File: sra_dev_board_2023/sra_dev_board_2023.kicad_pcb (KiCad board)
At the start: 2 copper layers, 81.2 x 92.7 mm, 201 parts, among them J1 Conn_01x19_Male, J10 Conn_01x03_Male, J11 Conn_01x05_Male, J12 Conn_01x05_Male, J13 Conn_01x05_Male, J14 Conn_01x03_Male, J15 Conn_01x03_Male, J16 Screw_Terminal_01x05, J17 Conn_01x06_Male, J2 Conn_01x03_Male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

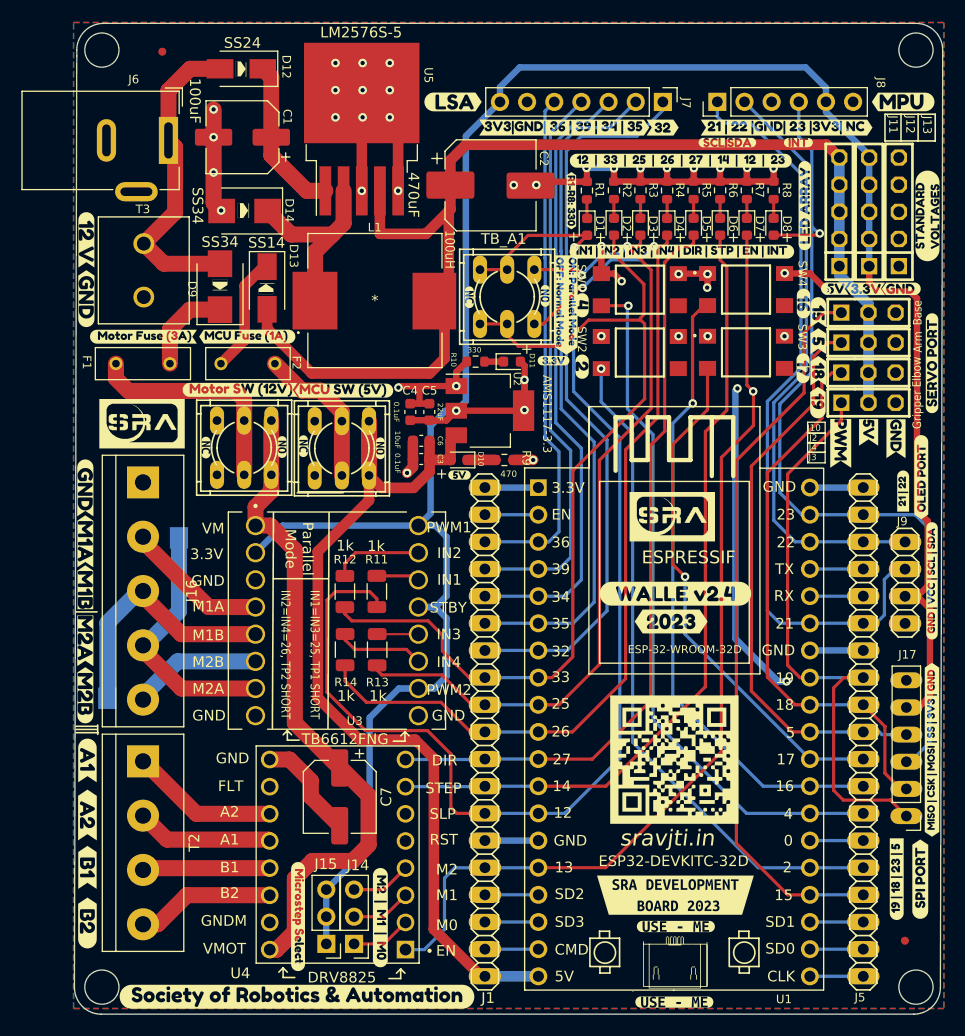
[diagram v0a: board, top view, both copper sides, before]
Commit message: Tweaks in routing prototype-1
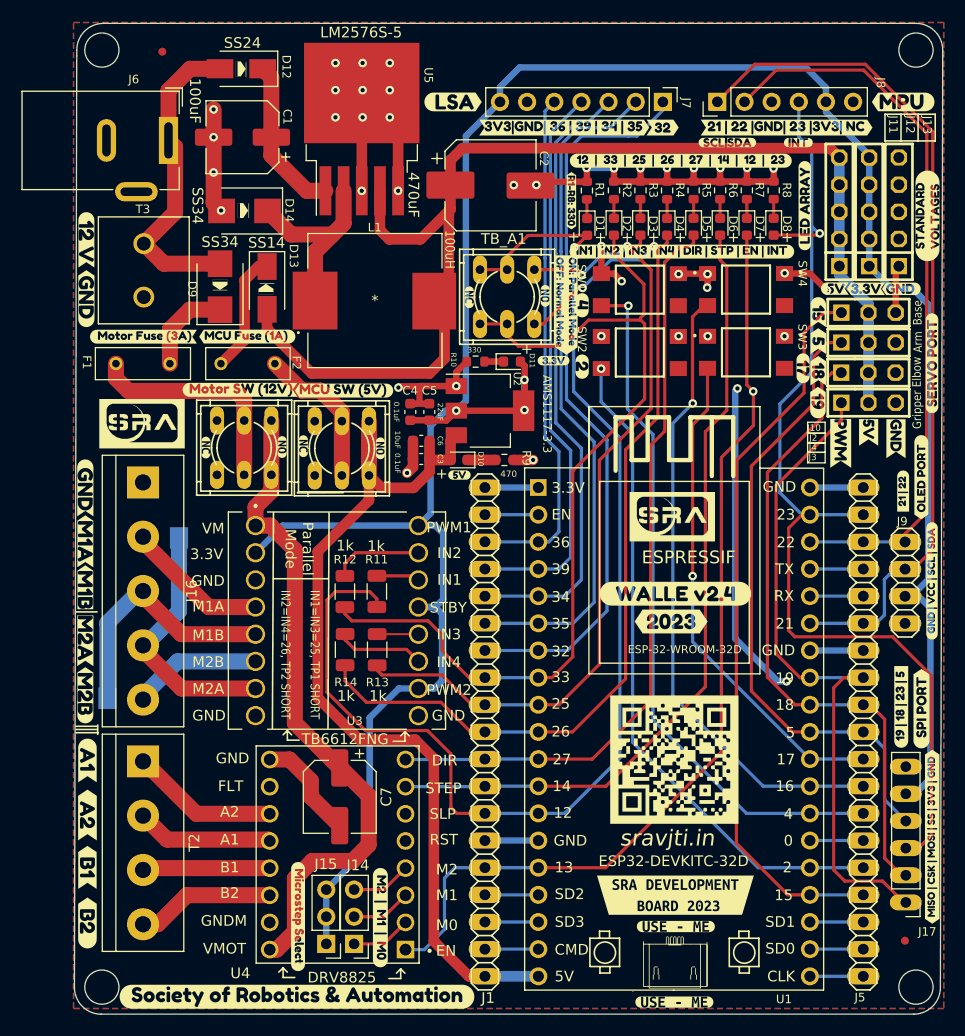
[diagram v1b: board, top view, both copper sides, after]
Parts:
- removed kibuzzard-61F6A06B: G***, kibuzzard-61F6A06B
- moved kibuzzard-637B65B8 16.7 mm to (147.2, 92.9)
- moved kibuzzard-637A1556 16.1 mm to (147.1, 93.4)
- moved kibuzzard-637A19A6 16.0 mm to (149.0, 93.5)
- moved kibuzzard-63777F1B 16.0 mm to (149.1, 93.5)
- moved kibuzzard-63775DBB 8.13 mm to (150.0, 105.5)
- moved kibuzzard-63775DBB 8.10 mm to (150.0, 105.5)
- moved J17 8.08 mm to (147.6, 111.7)
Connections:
- net /21 renamed D+
- net /22 renamed D-
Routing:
- net /23: track 82.2 -> 97.6 mm
- net D-: track 55.9 -> 68.7 mm
- net D+: track 71.0 -> 80.0 mm
- net /19: track 54.8 -> 63.3 mm
- net /18: track 51.7 -> 60.1 mm
- net /3V3: track 230.8 -> 238.4 mm
- net /5: track 53.0 -> 59.1 mm
- net GND: track 148.3 -> 152.6 mm
- net /17: track 48.2 -> 46.7 mm
- net /5V_P: track 82.8 -> 83.5 mm

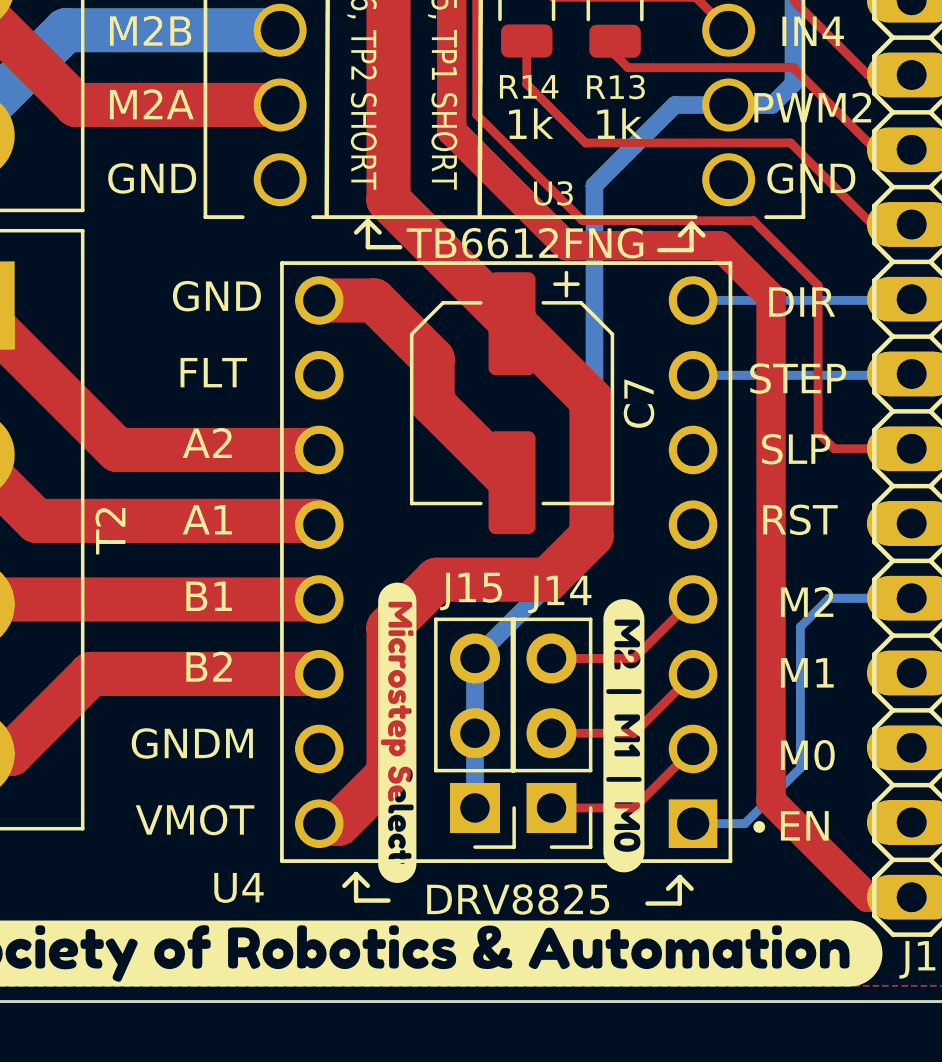
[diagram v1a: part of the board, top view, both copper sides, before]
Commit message: Update LSA and SRA board after hardware testing
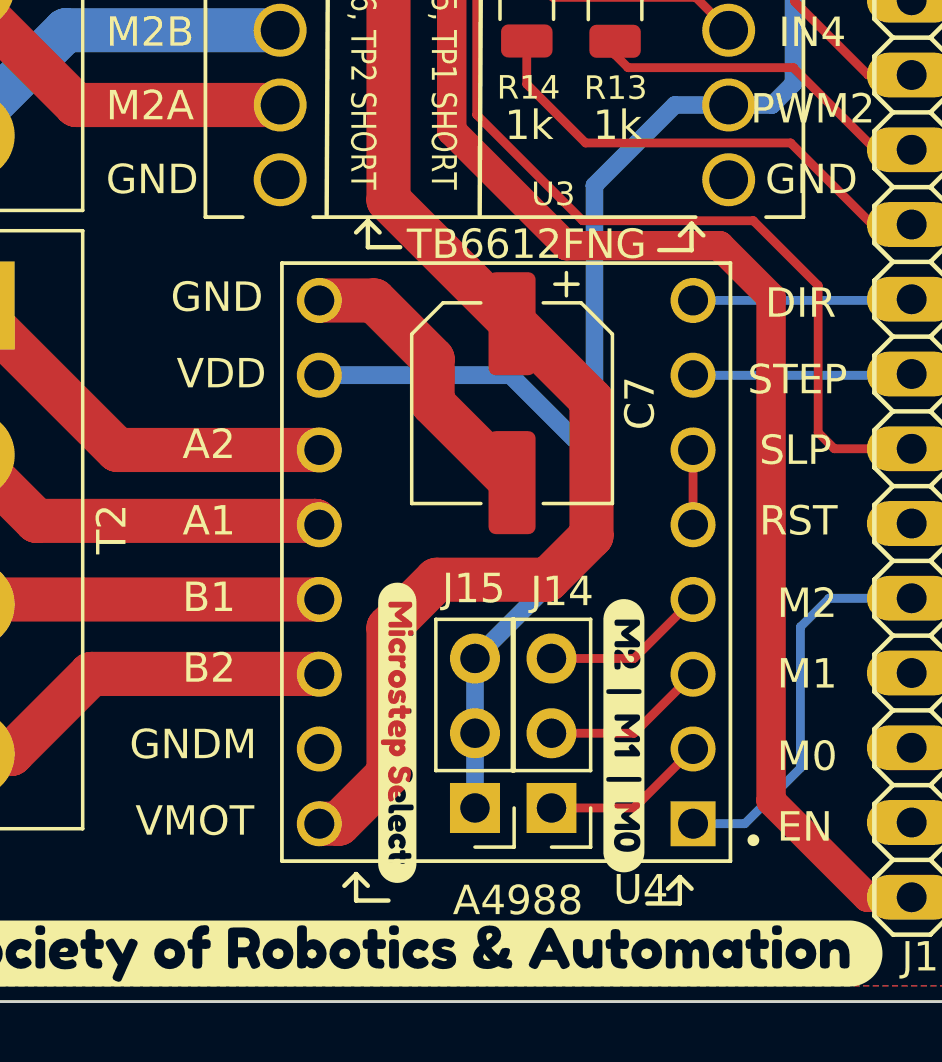
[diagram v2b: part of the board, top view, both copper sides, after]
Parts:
- U4: value DRV8825_STEPPER_MOTOR_DRIVER_CARRIER -> A4988_STEPPER_MOTOR_DRIVER_CARRIER; footprint stepper_motor_driver:IC_DRV8825_STEPPER_MOTOR_DRIVER_CARRIER -> stepper_motor_driver:MODULE_A4988_STEPPER_MOTOR_DRIVER_CARRIER
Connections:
- U4 pad 10: unconnected-(U4-Pad10) -> /3V3
- U4 pad 5: unconnected-(U4-Pad5) -> Net-(U4-Pad5)
- U4 pad 6: unconnected-(U4-Pad6) -> Net-(U4-Pad5)
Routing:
- net /3V3: track 238.4 -> 249.0 mm
- net Net-(U4-Pad5): track 0.00 -> 2.54 mm
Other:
- board text added: "A4988"
- board text added: "VDD"
- board text removed: "DRV8825"

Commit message: Update repo with recent changes
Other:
- board text removed: "FLT"
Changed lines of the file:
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@@
     (effects (font (size 1 1) (thickness 0.25)) (justify left mirror))
   )
-  (gr_text "FLT" (at 84.8 100.8) (layer "B.SilkS")
+  (gr_text "VDD" (at 84.8 100.8) (layer "B.SilkS")
     (effects (font (size 1 1) (thickness 0.25)) (justify left mirror))
   )
